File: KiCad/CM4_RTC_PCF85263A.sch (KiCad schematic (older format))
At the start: 0 parts

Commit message: added RTC circuit
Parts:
- added BT?: Battery_Cell, CM4_MATX:BatteryHolder_Keystone_103_1x20mm, symbol CM4_MATX:Battery_Cell
- added C? (x2): C100n, CM4_MATX:C_0805_2012Metric_Pad1.18x1.45mm_HandSolder, symbol CM4_MATX:C
- added R? (x2): R1.1k, CM4_MATX:R_0805_2012Metric_Pad1.20x1.40mm_HandSolder, symbol CM4_MATX:R
- added U?: PCF85263AT, CM4_MATX:SO-8_3.9x4.9mm_P1.27mm, symbol CM4_MATX:PCF85263AT
- added Y?: Crystal, CM4_MATX:Crystal_SMD_MicroCrystal_CC7V-T1A-2Pin_3.2x1.5mm_HandSoldering, symbol CM4_MATX:Crystal
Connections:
- new net +5v: C?.1, R?.1, R?.1, U?.8 (VDD)
- new net GND: BT?.2 (-), C?.2, C?.2, U?.4 (VSS)
- new net OSCI: U?.1 (OSCI), Y?.1
- new net OSCO: U?.2 (OSCO), Y?.2
- new net SCL: R?.2, U?.6 (SCL)
- new net SDA: R?.2, U?.5 (SDA)
- new net VBAT: BT?.1 (+), C?.1, U?.3 (VBAT)
- no-connect marks 0 -> 1
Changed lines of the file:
@@
 Comment4 ""
 $EndDescr
+$Comp
+L CM4_MATX:PCF85263AT U?
+U 1 1 5FF1EFD6
+P 5350 3350
+F 0 "U?" H 5894 3396 50  0000 L CNN
+F 1 "PCF85263AT" H 5894 3305 50  0000 L CNN
+F 2 "CM4_MATX:SO-8_3.9x4.9mm_P1.27mm" H 5350 2500 50  0001 C CNN
+F 3 "https://www.nxp.com/docs/en/data-sheet/PCF85263A.pdf" H 5350 3150 50  0001 C CNN
+F 4 "771-PCF85263AT/AJ" H 5350 2400 50  0001 C CNN "Mouser No"
+F 5 "PCF85263AT/AJ" H 5350 2300 50  0001 C CNN "Mfr. No"
+F 6 "NXP Semiconductors" H 5350 2200 50  0001 C CNN "Mfr."
+	1    5350 3350
+	1    0    0    -1
+$EndComp
+$Comp
+L CM4_MATX:GND #PWR?
+U 1 1 5FF1FFCE
+P 5350 3950
+F 0 "#PWR?" H 5350 3700 50  0001 C CNN
+F 1 "GND" H 5355 3777 50  0000 C CNN
+F 2 "" H 5350 3950 50  0001 C CNN
+F 3 "" H 5350 3950 50  0001 C CNN
+	1    5350 3950
+	1    0    0    -1
+$EndComp
+$Comp
+L CM4_MATX:C C?
+U 1 1 5FF203BF
+P 4850 2450
+F 0 "C?" H 4965 2496 50  0000 L CNN
+F 1 "C100n" H 4965 2405 50  0000 L CNN
+F 2 "CM4_MATX:C_0805_2012Metric_Pad1.18x1.45mm_HandSolder" H 4888 2300 50  0001 C CNN
+F 3 "~" H 4850 2450 50  0001 C CNN
+	1    4850 2450
+	1    0    0    -1
+$EndComp
+Wire Wire Line
+	5350 3750 5350 3950
+Text Label 4700 3150 0    50   ~ 0
+SCL
+Text Label 4700 3250 0    50   ~ 0
+SDA
+Text Label 5350 3850 0    50   ~ 0
+GND
+Text HLabel 3650 3150 0    50   Input ~ 0
+SCL
+Text HLabel 3650 3250 0    50   Input ~ 0
+SDA
+Text HLabel 4900 1750 0    50   Input ~ 0
++5v
+Wire Wire Line
+	4850 2200 4850 2300
+$Comp
+L CM4_MATX:GND #PWR?
+U 1 1 5FF245B2
+P 4850 2650
+F 0 "#PWR?" H 4850 2400 50  0001 C CNN
+F 1 "GND" H 4855 2477 50  0000 C CNN
+F 2 "" H 4850 2650 50  0001 C CNN
+F 3 "" H 4850 2650 50  0001 C CNN
+	1    4850 2650
+	1    0    0    -1
+$EndComp
+Wire Wire Line
+	4850 2600 4850 2650
+Wire Wire Line
+	4850 2200 5250 2200
+Wire Wire Line
+	5250 2200 5250 2950
+$Comp
+L CM4_MATX:Battery_Cell BT?
+U 1 1 5FF34AE7
+P 5650 2500
+F 0 "BT?" H 5768 2596 50  0000 L CNN
+F 1 "Battery_Cell" H 5768 2505 50  0000 L CNN
+F 2 "CM4_MATX:BatteryHolder_Keystone_103_1x20mm" V 5650 2560 50  0001 C CNN
+F 3 "https://www.mouser.dk/datasheet/2/215/03-745368.pdf" V 5650 2560 50  0001 C CNN
+F 4 "534-103" H 5650 2500 50  0001 C CNN "Mouser No"
+F 5 "103" H 5650 2500 50  0001 C CNN "Mfr. No"
+F 6 "Keystone Electronics" H 5650 2500 50  0001 C CNN "Mfr."
+	1    5650 2500
+	1    0    0    -1
+$EndComp
+$Comp
+L CM4_MATX:C C?
+U 1 1 5FF35A32
+P 6350 2450
+F 0 "C?" H 6465 2496 50  0000 L CNN
+F 1 "C100n" H 6465 2405 50  0000 L CNN
+F 2 "CM4_MATX:C_0805_2012Metric_Pad1.18x1.45mm_HandSolder" H 6388 2300 50  0001 C CNN
+F 3 "~" H 6350 2450 50  0001 C CNN
+	1    6350 2450
+	1    0    0    -1
+$EndComp
+Wire Wire Line
+	5350 2950 5350 2200
+Wire Wire Line
+	5350 2200 5650 2200
+Wire Wire Line
+	6350 2200 6350 2300
+Wire Wire Line
+	5650 2300 5650 2200
+Connection ~ 5650 2200
+Wire Wire Line
+	5650 2200 6350 2200
+Wire Wire Line
+	5650 2600 5650 2700
+Wire Wire Line
+	5650 2700 6350 2700
+Wire Wire Line
+	6350 2700 6350 2600
+Wire Wire Line
+	6350 2700 6350 2800
+Connection ~ 6350 2700
+$Comp
+L CM4_MATX:GND #PWR?
+U 1 1 5FF369EA
+P 6350 2800
+F 0 "#PWR?" H 6350 2550 50  0001 C CNN
+F 1 "GND" H 6355 2627 50  0000 C CNN
+F 2 "" H 6350 2800 50  0001 C CNN
+F 3 "" H 6350 2800 50  0001 C CNN
+	1    6350 2800
+	1    0    0    -1
+$EndComp
+Text Label 5850 2200 0    50   ~ 0
+VBAT
+Text Label 5850 2700 0    50   ~ 0
+GND
+Text Label 5250 2700 2    50   ~ 0
+VDD
+NoConn ~ 5850 3250
+Wire Wire Line
+	3650 3150 3900 3150
+Wire Wire Line
+	3650 3250 4300 3250
+Connection ~ 4850 2200
+Connection ~ 4300 3250
+Wire Wire Line
+	4300 3250 4850 3250
+$Comp
+L CM4_MATX:R R?
+U 1 1 5FF45F87
+P 3900 2450
+F 0 "R?" H 3970 2496 50  0000 L CNN
+F 1 "R1.1k" H 3970 2405 50  0000 L CNN
+F 2 "CM4_MATX:R_0805_2012Metric_Pad1.20x1.40mm_HandSolder" V 3830 2450 50  0001 C CNN
+F 3 "~" H 3900 2450 50  0001 C CNN
+	1    3900 2450
+	1    0    0    -1
+$EndComp
+$Comp
+L CM4_MATX:R R?
+U 1 1 5FF4821C
+P 4300 2450
+F 0 "R?" H 4370 2496 50  0000 L CNN
+F 1 "R1.1k" H 4370 2405 50  0000 L CNN
+F 2 "CM4_MATX:R_0805_2012Metric_Pad1.20x1.40mm_HandSolder" V 4230 2450 50  0001 C CNN
+F 3 "~" H 4300 2450 50  0001 C CNN
+	1    4300 2450
+	1    0    0    -1
+$EndComp
+Wire Wire Line
+	3900 2600 3900 3150
+Wire Wire Line
+	3900 2200 3900 2300
+Wire Wire Line
+	4300 2200 4300 2300
+Connection ~ 4300 2200
+Wire Wire Line
+	4300 2200 4850 2200
+Wire Wire Line
+	4300 2600 4300 3250
+Connection ~ 3900 3150
+Wire Wire Line
+	3900 3150 4850 3150
+Wire Wire Line
+	3900 2200 4300 2200
+$Comp
+L CM4_MATX:Crystal Y?
+U 1 1 5FF8A2E4
+P 4200 3700
+F 0 "Y?" V 4154 3831 50  0000 L CNN
+F 1 "Crystal" V 4245 3831 50  0000 L CNN
+F 2 "CM4_MATX:Crystal_SMD_MicroCrystal_CC7V-T1A-2Pin_3.2x1.5mm_HandSoldering" H 4200 3700 50  0001 C CNN
+F 3 "https://www.mouser.dk/datasheet/2/530/cc7v-t1a-1085773.pdf" H 4200 3700 50  0001 C CNN
+F 4 "428-200006-MG01" V 4200 3700 50  0001 C CNN "Mouser No"
+F 5 "Micro Crystal" V 4200 3700 50  0001 C CNN "Mfr."
+F 6 "CC7V-T1A-32.768kHz-12.5pF-20PPM-TA-QC" V 4200 3700 50  0001 C CNN "Mfr. No"
+F 7 "Crystals 32.768 kHz 12.5 pF +/-20 PPM -40/+85C" V 4200 3700 50  0001 C CNN "Descripton"
+	1    4200 3700
+	0    1    1    0
+$EndComp
+Wire Wire Line
+	4200 3450 4200 3550
+Wire Wire Line
+	4850 3550 4750 3550
+Wire Wire Line
+	4750 3550 4750 4000
+Wire Wire Line
+	4750 4000 4200 4000
+Wire Wire Line
+	4200 4000 4200 3850
+Wire Wire Line
+	4200 3450 4850 3450
+Text Label 4350 3450 0    50   ~ 0
+OSCI
+Text Label 4350 4000 0    50   ~ 0
+OSCO
+Wire Wire Line
+	4900 1750 5250 1750
+Wire Wire Line
+	5250 1750 5250 2200
+Connection ~ 5250 2200
 $EndSCHEMATC

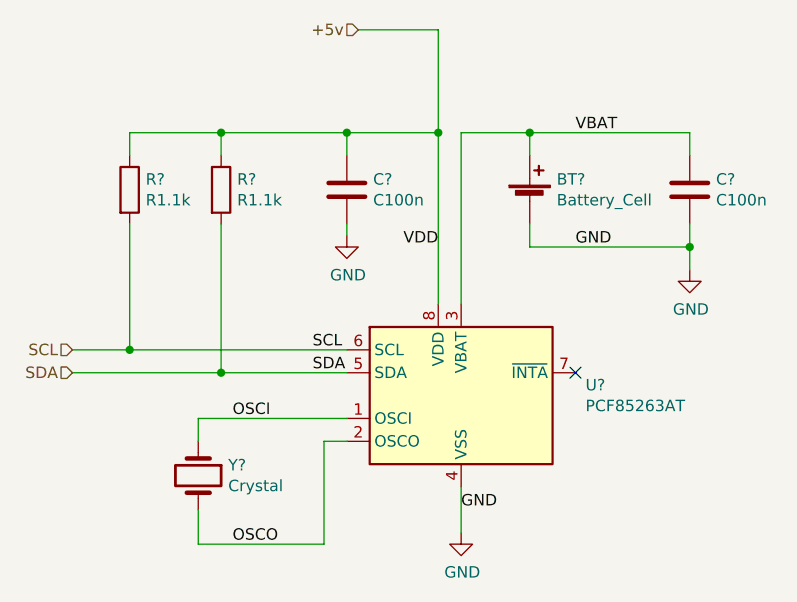
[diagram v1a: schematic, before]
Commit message: updated PCB with RTC circuit
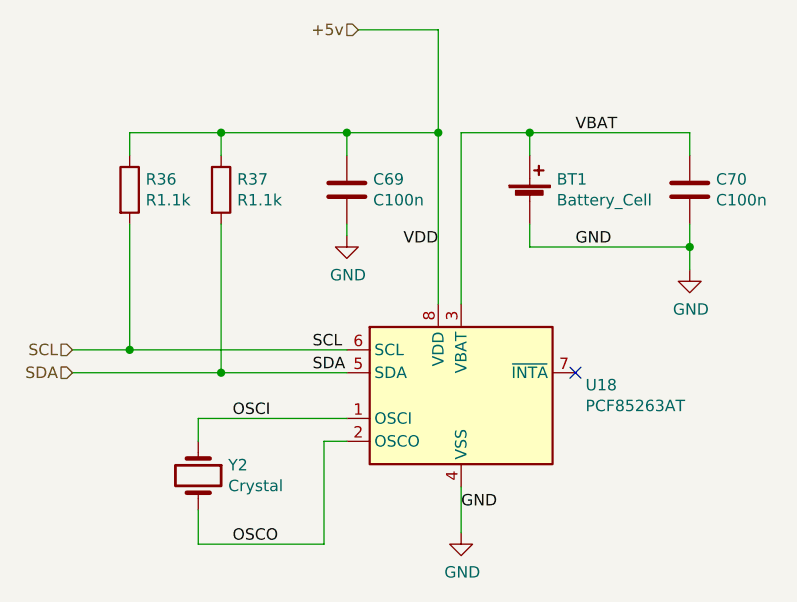
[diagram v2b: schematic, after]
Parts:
- gave numbers to parts that had none: 7
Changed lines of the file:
@@
 $EndDescr
 $Comp
-L CM4_MATX:PCF85263AT U?
+L CM4_MATX:PCF85263AT U18
 U 1 1 5FF1EFD6
 P 5350 3350
-F 0 "U?" H 5894 3396 50  0000 L CNN
+F 0 "U18" H 5894 3396 50  0000 L CNN
 F 1 "PCF85263AT" H 5894 3305 50  0000 L CNN
 F 2 "CM4_MATX:SO-8_3.9x4.9mm_P1.27mm" H 5350 2500 50  0001 C CNN
@@
 $EndComp
 $Comp
-L CM4_MATX:GND #PWR?
+L CM4_MATX:GND #PWR0220
 U 1 1 5FF1FFCE
 P 5350 3950
-F 0 "#PWR?" H 5350 3700 50  0001 C CNN
+F 0 "#PWR0220" H 5350 3700 50  0001 C CNN
 F 1 "GND" H 5355 3777 50  0000 C CNN
 F 2 "" H 5350 3950 50  0001 C CNN
@@
 $EndComp
 $Comp
-L CM4_MATX:C C?
+L CM4_MATX:C C69
 U 1 1 5FF203BF
 P 4850 2450
-F 0 "C?" H 4965 2496 50  0000 L CNN
+F 0 "C69" H 4965 2496 50  0000 L CNN
 F 1 "C100n" H 4965 2405 50  0000 L CNN
 F 2 "CM4_MATX:C_0805_2012Metric_Pad1.18x1.45mm_HandSolder" H 4888 2300 50  0001 C CNN
@@
 	4850 2200 4850 2300
 $Comp
-L CM4_MATX:GND #PWR?
+L CM4_MATX:GND #PWR0221
 U 1 1 5FF245B2
 P 4850 2650
-F 0 "#PWR?" H 4850 2400 50  0001 C CNN
+F 0 "#PWR0221" H 4850 2400 50  0001 C CNN
 F 1 "GND" H 4855 2477 50  0000 C CNN
 F 2 "" H 4850 2650 50  0001 C CNN
@@
 	5250 2200 5250 2950
 $Comp
-L CM4_MATX:Battery_Cell BT?
+L CM4_MATX:Battery_Cell BT1
 U 1 1 5FF34AE7
 P 5650 2500
-F 0 "BT?" H 5768 2596 50  0000 L CNN
+F 0 "BT1" H 5768 2596 50  0000 L CNN
 F 1 "Battery_Cell" H 5768 2505 50  0000 L CNN
 F 2 "CM4_MATX:BatteryHolder_Keystone_103_1x20mm" V 5650 2560 50  0001 C CNN
@@
 $EndComp
 $Comp
-L CM4_MATX:C C?
+L CM4_MATX:C C70
 U 1 1 5FF35A32
 P 6350 2450
-F 0 "C?" H 6465 2496 50  0000 L CNN
+F 0 "C70" H 6465 2496 50  0000 L CNN
 F 1 "C100n" H 6465 2405 50  0000 L CNN
 F 2 "CM4_MATX:C_0805_2012Metric_Pad1.18x1.45mm_HandSolder" H 6388 2300 50  0001 C CNN
@@
 Connection ~ 6350 2700
 $Comp
-L CM4_MATX:GND #PWR?
+L CM4_MATX:GND #PWR0222
 U 1 1 5FF369EA
 P 6350 2800
-F 0 "#PWR?" H 6350 2550 50  0001 C CNN
+F 0 "#PWR0222" H 6350 2550 50  0001 C CNN
 F 1 "GND" H 6355 2627 50  0000 C CNN
 F 2 "" H 6350 2800 50  0001 C CNN
@@
 	4300 3250 4850 3250
 $Comp
-L CM4_MATX:R R?
+L CM4_MATX:R R36
 U 1 1 5FF45F87
 P 3900 2450
-F 0 "R?" H 3970 2496 50  0000 L CNN
+F 0 "R36" H 3970 2496 50  0000 L CNN
 F 1 "R1.1k" H 3970 2405 50  0000 L CNN
 F 2 "CM4_MATX:R_0805_2012Metric_Pad1.20x1.40mm_HandSolder" V 3830 2450 50  0001 C CNN
@@
 $EndComp
 $Comp
-L CM4_MATX:R R?
+L CM4_MATX:R R37
 U 1 1 5FF4821C
 P 4300 2450
-F 0 "R?" H 4370 2496 50  0000 L CNN
+F 0 "R37" H 4370 2496 50  0000 L CNN
 F 1 "R1.1k" H 4370 2405 50  0000 L CNN
 F 2 "CM4_MATX:R_0805_2012Metric_Pad1.20x1.40mm_HandSolder" V 4230 2450 50  0001 C CNN
@@
 	3900 2200 4300 2200
 $Comp
-L CM4_MATX:Crystal Y?
+L CM4_MATX:Crystal Y2
 U 1 1 5FF8A2E4
 P 4200 3700
-F 0 "Y?" V 4154 3831 50  0000 L CNN
+F 0 "Y2" V 4154 3831 50  0000 L CNN
 F 1 "Crystal" V 4245 3831 50  0000 L CNN
 F 2 "CM4_MATX:Crystal_SMD_MicroCrystal_CC7V-T1A-2Pin_3.2x1.5mm_HandSoldering" H 4200 3700 50  0001 C CNN

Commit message: removed i2c pull-up resistors to +5v
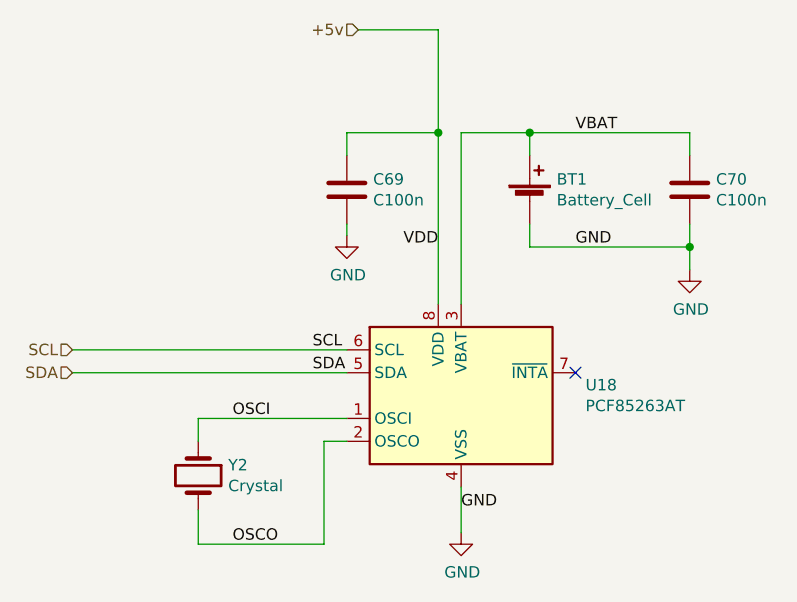
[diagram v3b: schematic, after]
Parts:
- removed R36, R37: R1.1k, CM4_MATX:R_0805_2012Metric_Pad1.20x1.40mm_HandSolder, symbol CM4_MATX:R
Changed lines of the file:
@@
 VDD
 NoConn ~ 5850 3250
-Wire Wire Line
-	3650 3150 3900 3150
-Wire Wire Line
-	3650 3250 4300 3250
-Connection ~ 4850 2200
-Connection ~ 4300 3250
-Wire Wire Line
-	4300 3250 4850 3250
-$Comp
-L CM4_MATX:R R36
-U 1 1 5FF45F87
-P 3900 2450
-F 0 "R36" H 3970 2496 50  0000 L CNN
-F 1 "R1.1k" H 3970 2405 50  0000 L CNN
-F 2 "CM4_MATX:R_0805_2012Metric_Pad1.20x1.40mm_HandSolder" V 3830 2450 50  0001 C CNN
-F 3 "~" H 3900 2450 50  0001 C CNN
-	1    3900 2450
-	1    0    0    -1
-$EndComp
-$Comp
-L CM4_MATX:R R37
-U 1 1 5FF4821C
-P 4300 2450
-F 0 "R37" H 4370 2496 50  0000 L CNN
-F 1 "R1.1k" H 4370 2405 50  0000 L CNN
-F 2 "CM4_MATX:R_0805_2012Metric_Pad1.20x1.40mm_HandSolder" V 4230 2450 50  0001 C CNN
-F 3 "~" H 4300 2450 50  0001 C CNN
-	1    4300 2450
-	1    0    0    -1
-$EndComp
-Wire Wire Line
-	3900 2600 3900 3150
-Wire Wire Line
-	3900 2200 3900 2300
-Wire Wire Line
-	4300 2200 4300 2300
-Connection ~ 4300 2200
-Wire Wire Line
-	4300 2200 4850 2200
-Wire Wire Line
-	4300 2600 4300 3250
-Connection ~ 3900 3150
-Wire Wire Line
-	3900 3150 4850 3150
-Wire Wire Line
-	3900 2200 4300 2200
 $Comp
 L CM4_MATX:Crystal Y2
@@
 	5250 1750 5250 2200
 Connection ~ 5250 2200
+Wire Wire Line
+	3650 3150 4850 3150
+Wire Wire Line
+	3650 3250 4850 3250
 $EndSCHEMATC

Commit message: PCIe Wiring, resistor value adjustments, and a bunch of small ERC fixes.
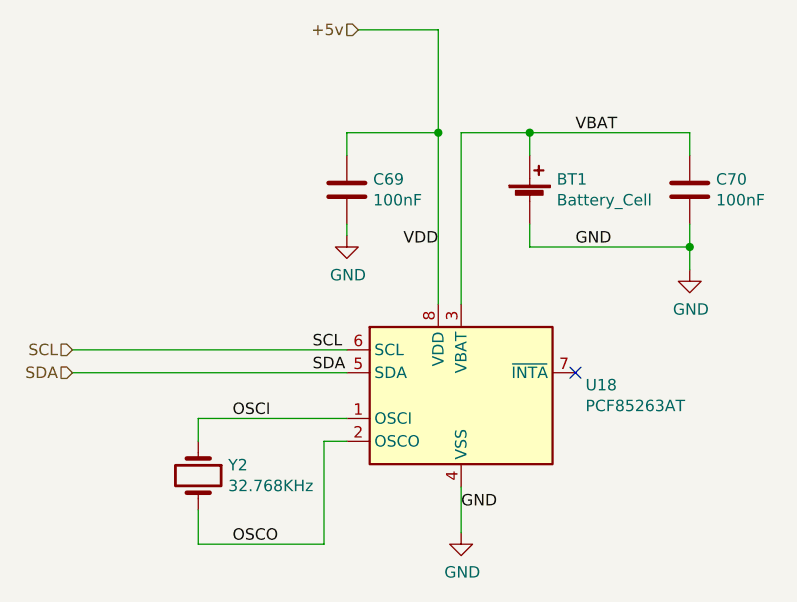
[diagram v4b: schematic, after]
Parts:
- C69, C70: value C100n -> 100nF
- Y2: value Crystal -> 32.768KHz
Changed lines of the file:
@@
 $Descr A4 11693 8268
 encoding utf-8
-Sheet 16 16
+Sheet 9 16
 Title ""
 Date ""
@@
 P 4850 2450
 F 0 "C69" H 4965 2496 50  0000 L CNN
-F 1 "C100n" H 4965 2405 50  0000 L CNN
+F 1 "100nF" H 4965 2405 50  0000 L CNN
 F 2 "CM4_MATX:C_0805_2012Metric_Pad1.18x1.45mm_HandSolder" H 4888 2300 50  0001 C CNN
 F 3 "~" H 4850 2450 50  0001 C CNN
@@
 P 6350 2450
 F 0 "C70" H 6465 2496 50  0000 L CNN
-F 1 "C100n" H 6465 2405 50  0000 L CNN
+F 1 "100nF" H 6465 2405 50  0000 L CNN
 F 2 "CM4_MATX:C_0805_2012Metric_Pad1.18x1.45mm_HandSolder" H 6388 2300 50  0001 C CNN
 F 3 "~" H 6350 2450 50  0001 C CNN
@@
 P 4200 3700
 F 0 "Y2" V 4154 3831 50  0000 L CNN
-F 1 "Crystal" V 4245 3831 50  0000 L CNN
+F 1 "32.768KHz" V 4245 3831 50  0000 L CNN
 F 2 "CM4_MATX:Crystal_SMD_MicroCrystal_CC7V-T1A-2Pin_3.2x1.5mm_HandSoldering" H 4200 3700 50  0001 C CNN
 F 3 "https://www.mouser.dk/datasheet/2/530/cc7v-t1a-1085773.pdf" H 4200 3700 50  0001 C CNN

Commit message: Started picking passive components, overhauled library
Cleaned up a bunch of schematic library references.
Added datasheets, descriptions for a lot of existing parts.
Picked most capacitor parts, still a couple left.
Cleaned up a fair few footprint references.
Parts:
- BT1: Description (none) -> CR2032 Battery Holder; Mouser No 534-103 -> (none); Mouser Part Number (none) -> 534-103; Mouser Price/Stock (none) -> https://www.mouser.co.uk/ProductDetail/Keystone-Electronics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
- C69, C70: footprint CM4_MATX:C_0805_2012Metric_Pad1.18x1.45mm_HandSolder -> CM4_MATX:C_0402_1005Metric_Pad0.74x0.62mm_HandSolder; Description (none) -> 10V 0.1uF X5R 0402 20% Tol; Mfr. (none) -> AVX; Mfr. No (none) -> 0402ZD104MAT4A; Mouser Part Number (none) -> 581-0402ZD104MAT4A; Mouser Price/Stock (none) -> https://www.mouser.co.uk/ProductDetail/AVX/0402ZD104MAT4A/?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
- U18: Description (none) -> Low Power Real time clock; Mouser No 771-PCF85263AT/AJ -> (none); Mouser Part Number (none) -> 771-PCF85263AT/AJ; Mouser Price/Stock (none) -> https://www.mouser.co.uk/ProductDetail/NXP-Semiconductors/P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
- Y2: Description (none) -> Crystals 32.768 kHz 12.5 pF +/-20 PPM -40/+85C; Descripton Crystals 32.768 kHz 12.5 pF +/-20 PPM -40/+85C -> (none); Mouser No 428-200006-MG01 -> (none); Mouser Part Number (none) -> 428-200006-MG01; Mouser Price/Stock (none) -> https://www.mouser.co.uk/ProductDetail/Micro-Crystal/CC7V-T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
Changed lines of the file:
@@
 F 2 "CM4_MATX:SO-8_3.9x4.9mm_P1.27mm" H 5350 2500 50  0001 C CNN
 F 3 "https://www.nxp.com/docs/en/data-sheet/PCF85263A.pdf" H 5350 3150 50  0001 C CNN
-F 4 "771-PCF85263AT/AJ" H 5350 2400 50  0001 C CNN "Mouser No"
-F 5 "PCF85263AT/AJ" H 5350 2300 50  0001 C CNN "Mfr. No"
-F 6 "NXP Semiconductors" H 5350 2200 50  0001 C CNN "Mfr."
+F 4 "PCF85263AT/AJ" H 5350 2300 50  0001 C CNN "Mfr. No"
+F 5 "NXP Semiconductors" H 5350 2200 50  0001 C CNN "Mfr."
+F 6 "771-PCF85263AT/AJ" H 5350 3350 50  0001 C CNN "Mouser Part Number"
+F 7 "https://www.mouser.co.uk/ProductDetail/NXP-Semiconductors/PCF85263AT-AJ/?qs=%2Fha2pyFadujHIZzLgxdeD%2FWcS1amNAs344JxIbLDsIJmxz87yr0P6tzLitY%2FwIc8" H 5350 3350 50  0001 C CNN "Mouser Price/Stock"
+F 8 "Low Power Real time clock" H 5350 3350 50  0001 C CNN "Description"
 	1    5350 3350
 	1    0    0    -1
@@
 F 0 "C69" H 4965 2496 50  0000 L CNN
 F 1 "100nF" H 4965 2405 50  0000 L CNN
-F 2 "CM4_MATX:C_0805_2012Metric_Pad1.18x1.45mm_HandSolder" H 4888 2300 50  0001 C CNN
-F 3 "~" H 4850 2450 50  0001 C CNN
+F 2 "CM4_MATX:C_0402_1005Metric_Pad0.74x0.62mm_HandSolder" H 4888 2300 50  0001 C CNN
+F 3 "https://www.mouser.co.uk/datasheet/2/40/cx5r-776519.pdf" H 4850 2450 50  0001 C CNN
+F 4 "581-0402ZD104MAT4A" H 4850 2450 50  0001 C CNN "Mouser Part Number"
+F 5 "https://www.mouser.co.uk/ProductDetail/AVX/0402ZD104MAT4A/?qs=sGAEpiMZZMvsSlwiRhF8qud6rLLpfNdE%2FYSoyEGdkn4%3D" H 4850 2450 50  0001 C CNN "Mouser Price/Stock"
+F 6 "AVX" H 4850 2450 50  0001 C CNN "Mfr."
+F 7 "0402ZD104MAT4A" H 4850 2450 50  0001 C CNN "Mfr. No"
+F 8 "10V 0.1uF X5R 0402 20% Tol" H 4850 2450 50  0001 C CNN "Description"
 	1    4850 2450
 	1    0    0    -1
@@
 F 2 "CM4_MATX:BatteryHolder_Keystone_103_1x20mm" V 5650 2560 50  0001 C CNN
 F 3 "https://www.mouser.dk/datasheet/2/215/03-745368.pdf" V 5650 2560 50  0001 C CNN
-F 4 "534-103" H 5650 2500 50  0001 C CNN "Mouser No"
-F 5 "103" H 5650 2500 50  0001 C CNN "Mfr. No"
-F 6 "Keystone Electronics" H 5650 2500 50  0001 C CNN "Mfr."
+F 4 "103" H 5650 2500 50  0001 C CNN "Mfr. No"
+F 5 "Keystone Electronics" H 5650 2500 50  0001 C CNN "Mfr."
+F 6 "534-103" H 5650 2500 50  0001 C CNN "Mouser Part Number"
+F 7 "https://www.mouser.co.uk/ProductDetail/Keystone-Electronics/103/?qs=Q3RoVmURDolsdXuDGYj49g%3D%3D" H 5650 2500 50  0001 C CNN "Mouser Price/Stock"
+F 8 "CR2032 Battery Holder" H 5650 2500 50  0001 C CNN "Description"
 	1    5650 2500
 	1    0    0    -1
@@
 F 0 "C70" H 6465 2496 50  0000 L CNN
 F 1 "100nF" H 6465 2405 50  0000 L CNN
-F 2 "CM4_MATX:C_0805_2012Metric_Pad1.18x1.45mm_HandSolder" H 6388 2300 50  0001 C CNN
-F 3 "~" H 6350 2450 50  0001 C CNN
+F 2 "CM4_MATX:C_0402_1005Metric_Pad0.74x0.62mm_HandSolder" H 6388 2300 50  0001 C CNN
+F 3 "https://www.mouser.co.uk/datasheet/2/40/cx5r-776519.pdf" H 6350 2450 50  0001 C CNN
+F 4 "581-0402ZD104MAT4A" H 6350 2450 50  0001 C CNN "Mouser Part Number"
+F 5 "https://www.mouser.co.uk/ProductDetail/AVX/0402ZD104MAT4A/?qs=sGAEpiMZZMvsSlwiRhF8qud6rLLpfNdE%2FYSoyEGdkn4%3D" H 6350 2450 50  0001 C CNN "Mouser Price/Stock"
+F 6 "AVX" H 6350 2450 50  0001 C CNN "Mfr."
+F 7 "0402ZD104MAT4A" H 6350 2450 50  0001 C CNN "Mfr. No"
+F 8 "10V 0.1uF X5R 0402 20% Tol" H 6350 2450 50  0001 C CNN "Description"
 	1    6350 2450
 	1    0    0    -1
@@
 F 2 "CM4_MATX:Crystal_SMD_MicroCrystal_CC7V-T1A-2Pin_3.2x1.5mm_HandSoldering" H 4200 3700 50  0001 C CNN
 F 3 "https://www.mouser.dk/datasheet/2/530/cc7v-t1a-1085773.pdf" H 4200 3700 50  0001 C CNN
-F 4 "428-200006-MG01" V 4200 3700 50  0001 C CNN "Mouser No"
-F 5 "Micro Crystal" V 4200 3700 50  0001 C CNN "Mfr."
-F 6 "CC7V-T1A-32.768kHz-12.5pF-20PPM-TA-QC" V 4200 3700 50  0001 C CNN "Mfr. No"
-F 7 "Crystals 32.768 kHz 12.5 pF +/-20 PPM -40/+85C" V 4200 3700 50  0001 C CNN "Descripton"
+F 4 "Micro Crystal" V 4200 3700 50  0001 C CNN "Mfr."
+F 5 "CC7V-T1A-32.768kHz-12.5pF-20PPM-TA-QC" V 4200 3700 50  0001 C CNN "Mfr. No"
+F 6 "Crystals 32.768 kHz 12.5 pF +/-20 PPM -40/+85C" V 4200 3700 50  0001 C CNN "Description"
+F 7 "428-200006-MG01" H 4200 3700 50  0001 C CNN "Mouser Part Number"
+F 8 "https://www.mouser.co.uk/ProductDetail/Micro-Crystal/CC7V-T1A-32768kHz-125pF-20PPM-TA-QC/?qs=%2Fha2pyFadug2yQXIRJoX08mUkRDjkgkyi7ZUDpZf0SmQho9ELDZmbA%3D%3D" H 4200 3700 50  0001 C CNN "Mouser Price/Stock"
 	1    4200 3700
 	0    1    1    0

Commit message: Connected all grounds in the schematic and planes
Planes:
In 1 - Ground
In 2 - 3.3v Zone which excludes the IO and 5v Zone around only the IO
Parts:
- added GND (x3): GND, symbol CM4_MATX:GND
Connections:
- net GND: now also GND.1 (GND), GND.1 (GND), GND.1 (GND)
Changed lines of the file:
@@
 $EndComp
 $Comp
-L CM4_MATX:GND #PWR0220
+L CM4_MATX:GND GND
 U 1 1 5FF1FFCE
 P 5350 3950
-F 0 "#PWR0220" H 5350 3700 50  0001 C CNN
+F 0 "GND" H 5350 3700 50  0001 C CNN
 F 1 "GND" H 5355 3777 50  0000 C CNN
 F 2 "" H 5350 3950 50  0001 C CNN
@@
 	4850 2200 4850 2300
 $Comp
-L CM4_MATX:GND #PWR0221
+L CM4_MATX:GND GND
 U 1 1 5FF245B2
 P 4850 2650
-F 0 "#PWR0221" H 4850 2400 50  0001 C CNN
+F 0 "GND" H 4850 2400 50  0001 C CNN
 F 1 "GND" H 4855 2477 50  0000 C CNN
 F 2 "" H 4850 2650 50  0001 C CNN
@@
 Connection ~ 6350 2700
 $Comp
-L CM4_MATX:GND #PWR0222
+L CM4_MATX:GND GND
 U 1 1 5FF369EA
 P 6350 2800
-F 0 "#PWR0222" H 6350 2550 50  0001 C CNN
+F 0 "GND" H 6350 2550 50  0001 C CNN
 F 1 "GND" H 6355 2627 50  0000 C CNN
 F 2 "" H 6350 2800 50  0001 C CNN
